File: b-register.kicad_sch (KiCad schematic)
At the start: 22 parts, among them U7 74HCT245, U8 74HCT173, U9 74HCT173

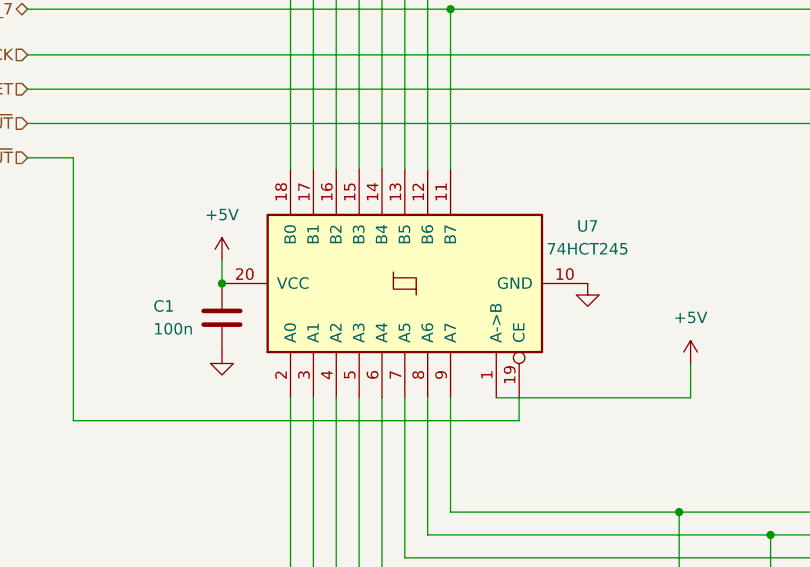
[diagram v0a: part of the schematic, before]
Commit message: changed symbols
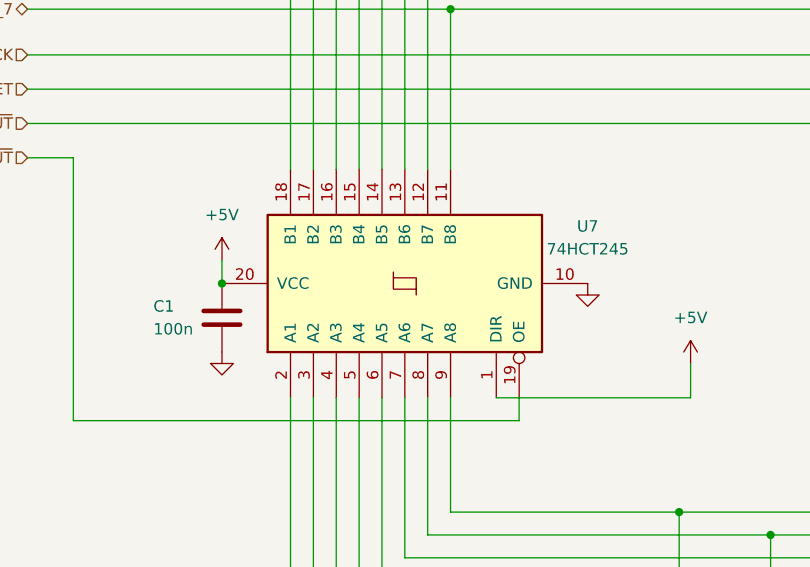
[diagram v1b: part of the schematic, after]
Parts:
- U7: symbol 74xx:74HC245 -> 01_my_library:74HCT245
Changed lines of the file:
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@@
     )
   )
-  (symbol (lib_id "74xx:74HC245") (at 72.39 72.39 90) (unit 1)
+  (symbol (lib_id "01_my_library:74HCT245") (at 72.39 72.39 90) (unit 1)
     (in_bom yes) (on_board yes) (dnp no)
     (property "Reference" "U7" (at 92.71 66.04 90)
@@
       (effects (font (size 1.27 1.27)) hide)
     )
-    (property "Datasheet" "http://www.ti.com/lit/gpn/sn74HC245" (at 72.39 72.39 0)
+    (property "Datasheet" "https://www.ti.com/lit/ds/symlink/sn74hct245.pdf?ts=1702763405638&ref_url=https%253A%252F%252Fwww.google.com%252F" (at 95.25 72.39 0)
       (effects (font (size 1.27 1.27)) hide)
     )

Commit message: cleanup
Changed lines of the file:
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@@
   (symbol (lib_id "74xx:74LS173") (at 148.59 72.39 270) (unit 1)
     (in_bom yes) (on_board yes) (dnp no) (fields_autoplaced)
-    (property "Reference" "U8" (at 171.45 65.4619 90)
+    (property "Reference" "U8" (at 172.72 65.4619 90)
       (effects (font (size 1.27 1.27)))
     )
-    (property "Value" "74HCT173" (at 171.45 68.0019 90)
+    (property "Value" "74HCT173" (at 172.72 68.0019 90)
       (effects (font (size 1.27 1.27)))
     )
@@
   (symbol (lib_id "74xx:74LS173") (at 223.52 72.39 270) (unit 1)
     (in_bom yes) (on_board yes) (dnp no) (fields_autoplaced)
-    (property "Reference" "U9" (at 246.38 65.4619 90)
+    (property "Reference" "U9" (at 247.65 65.4619 90)
       (effects (font (size 1.27 1.27)))
     )
-    (property "Value" "74HCT173" (at 246.38 68.0019 90)
+    (property "Value" "74HCT173" (at 247.65 68.0019 90)
       (effects (font (size 1.27 1.27)))
     )

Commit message: readme
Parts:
- added C13: 10n, 01_my_library:C_Disc_D4.0mm_W2.6mm_P2.50mm, symbol Device:C
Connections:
- net GND: now also C13.2
- net RESET: now also C13.1
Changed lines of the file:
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@@
   (junction (at 163.83 123.19) (diameter 0) (color 0 0 0 0)
   )
+  (junction (at 208.28 50.8) (diameter 0) (color 255 0 0 1)
+  )
   (junction (at 180.34 72.39) (diameter 0) (color 0 0 0 0)
   )
@@
     (stroke (width 0) (type default))
   )
+  (wire (pts (xy 208.28 34.29) (xy 219.71 34.29))
+    (stroke (width 0) (type default) (color 255 0 0 1))
+  )
   (wire (pts (xy 218.44 54.61) (xy 215.9 54.61))
     (stroke (width 0) (type default) (color 255 0 0 1))
@@
     (stroke (width 0) (type default))
   )
+  (wire (pts (xy 208.28 50.8) (xy 208.28 34.29))
+    (stroke (width 0) (type default) (color 255 0 0 1))
+  )
   (wire (pts (xy 59.69 85.09) (xy 59.69 115.57))
     (stroke (width 0) (type default))
@@
   (wire (pts (xy 180.34 69.85) (xy 180.34 72.39))
     (stroke (width 0) (type default))
+  )
+  (wire (pts (xy 219.71 34.29) (xy 219.71 38.1))
+    (stroke (width 0) (type default) (color 255 0 0 1))
   )
   (wire (pts (xy 153.67 125.73) (xy 153.67 143.51))
@@
         (path "/100bb8d1-c3d6-4e1f-87b6-72e4e187243c/3568514a-e420-48fa-9fd5-7a290120765b"
           (reference "#PWR057") (unit 1)
+        )
+      )
+    )
+  )
+  (symbol (lib_id "Device:C") (at 219.71 41.91 0) (unit 1)
+    (in_bom yes) (on_board yes) (dnp yes) (fields_autoplaced)
+    (property "Reference" "C13" (at 223.52 40.64 0)
+      (effects (font (size 1.27 1.27)) (justify left))
+    )
+    (property "Value" "10n" (at 223.52 43.18 0)
+      (effects (font (size 1.27 1.27)) (justify left))
+    )
+    (property "Footprint" "01_my_library:C_Disc_D4.0mm_W2.6mm_P2.50mm" (at 220.6752 45.72 0)
+      (effects (font (size 1.27 1.27)) hide)
+    )
+    (property "Datasheet" "~" (at 219.71 41.91 0)
+      (effects (font (size 1.27 1.27)) hide)
+    )
+    (pin "1")
+    (pin "2")
+    (instances
+      (project "8-bit-cpu"
+        (path "/100bb8d1-c3d6-4e1f-87b6-72e4e187243c/651dfbaf-e340-4976-8216-793c5a5aaa3b"
+          (reference "C13") (unit 1)
+        )
+        (path "/100bb8d1-c3d6-4e1f-87b6-72e4e187243c/3568514a-e420-48fa-9fd5-7a290120765b"
+          (reference "C76") (unit 1)
         )
       )
@@
         )
       )
+    )
+  )
+  (symbol (lib_id "power:GND") (at 219.71 45.72 0) (unit 1)
+    (in_bom yes) (on_board yes) (dnp no) (fields_autoplaced)
+    (property "Reference" "#PWR03" (at 219.71 52.07 0)
+      (effects (font (size 1.27 1.27)) hide)
+    )
+    (property "Value" "GND" (at 219.71 50.8 0)
+      (effects (font (size 1.27 1.27)) hide)
+    )
+    (property "Footprint" "" (at 219.71 45.72 0)
+      (effects (font (size 1.27 1.27)) hide)
+    )
+    (property "Datasheet" "" (at 219.71 45.72 0)
+      (effects (font (size 1.27 1.27)) hide)
+    )
+    (pin "1")
+    (instances
+      (project "8-bit-cpu"
+        (path "/100bb8d1-c3d6-4e1f-87b6-72e4e187243c/45eb39c3-c748-461e-8330-08aae1247dee"
+          (reference "#PWR03") (unit 1)
+        )
+        (path "/100bb8d1-c3d6-4e1f-87b6-72e4e187243c/651dfbaf-e340-4976-8216-793c5a5aaa3b"
+          (reference "#PWR038") (unit 1)
+        )
+        (path "/100bb8d1-c3d6-4e1f-87b6-72e4e187243c/3568514a-e420-48fa-9fd5-7a290120765b"
+          (reference "#PWR0264") (unit 1)
+        )
+      )

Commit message: kicad update
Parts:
- D21: renamed from D5; footprint LED_THT:LED_D5.0mm -> 01_my_library:LED_D5.0mm
- D22: renamed from D6; footprint LED_THT:LED_D5.0mm -> 01_my_library:LED_D5.0mm
- D23: renamed from D7; footprint LED_THT:LED_D5.0mm -> 01_my_library:LED_D5.0mm
- D24: renamed from D8; footprint LED_THT:LED_D5.0mm -> 01_my_library:LED_D5.0mm
- D25: renamed from D9; footprint LED_THT:LED_D5.0mm -> 01_my_library:LED_D5.0mm
- D26: renamed from D10; footprint LED_THT:LED_D5.0mm -> 01_my_library:LED_D5.0mm
- D27: renamed from D11; footprint LED_THT:LED_D5.0mm -> 01_my_library:LED_D5.0mm
- D28: renamed from D12; footprint LED_THT:LED_D5.0mm -> 01_my_library:LED_D5.0mm
- renumbered C13 to C17, C1 to C18, C1 to C19, C1 to C20, R11 to R35, R12 to R36, R13 to R37, R14 to R38, R15 to R39, R16 to R40, R17 to R41, R18 to R42, U7 to U10, U8 to U11, U9 to U12
